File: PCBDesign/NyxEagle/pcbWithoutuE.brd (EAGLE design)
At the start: 100 x 80 mm, 17 parts, among them IC1 DRV8304SRHAR

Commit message: Update pcbWithoutuE.brd and pcbWithoutuE.sch
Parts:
- added IN, IN1, JP1, SPI: (no value), jumper:JP4
- R1, R2: value 10k -> 5.1k
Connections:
- new net CAL: IC1.31, JP1.1
- new net ENABLE: IC1.30, JP1.2
- new net INHA: IC1.34, IN.1
- new net INHB: IC1.36, IN.3
- new net INHC: IC1.38, IN1.1
- new net INLA: IC1.35, IN.2
- new net INLB: IC1.37, IN.4
- new net INLC: IC1.39, IN1.2
- new net N$6: IN1.3
- new net N$7: JP1.4
- new net N$8: IN1.4
- new net NSCS: IC1.29, SPI.1
- new net SCLK: IC1.28, SPI.2
- new net SDI: IC1.27, SPI.3
- net NFAULT: now also JP1.3
- net SDO: now also SPI.4
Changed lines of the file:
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@@
 <attribute name="SPICEPREFIX" value="C" x="2.54" y="-20.32" size="1.778" layer="27" display="off"/>
 </element>
-<element name="R1" library="rcl" library_urn="urn:adsk.eagle:library:334" package="R0805" package3d_urn="urn:adsk.eagle:package:23553/2" value="10k" x="2.54" y="-26.67">
+<element name="R1" library="rcl" library_urn="urn:adsk.eagle:library:334" package="R0805" package3d_urn="urn:adsk.eagle:package:23553/2" value="5.1k" x="2.54" y="-26.67">
 <attribute name="SPICEPREFIX" value="R" x="2.54" y="-26.67" size="1.778" layer="27" display="off"/>
 </element>
@@
 <attribute name="SPICEPREFIX" value="C" x="2.54" y="-33.02" size="1.778" layer="27" display="off"/>
 </element>
-<element name="R2" library="rcl" library_urn="urn:adsk.eagle:library:334" package="R0805" package3d_urn="urn:adsk.eagle:package:23553/2" value="10k" x="2.54" y="-39.37">
+<element name="R2" library="rcl" library_urn="urn:adsk.eagle:library:334" package="R0805" package3d_urn="urn:adsk.eagle:package:23553/2" value="5.1k" x="2.54" y="-39.37">
 <attribute name="SPICEPREFIX" value="R" x="2.54" y="-39.37" size="1.778" layer="27" display="off"/>
 </element>
@@
 <element name="U$5" library="SamacSys_Parts2" package="SI7852ADPT1GE3" value="SIRA80DP-T1-RE3-CLASSIC" x="-25.4" y="-90.17"/>
 <element name="U$6" library="SamacSys_Parts2" package="SI7852ADPT1GE3" value="SIRA80DP-T1-RE3-CLASSIC" x="-33.02" y="-97.79"/>
+<element name="JP1" library="jumper" library_urn="urn:adsk.eagle:library:252" package="JP4" package3d_urn="urn:adsk.eagle:package:15463/1" value="" x="-39.37" y="-105.41"/>
+<element name="SPI" library="jumper" library_urn="urn:adsk.eagle:library:252" package="JP4" package3d_urn="urn:adsk.eagle:package:15463/1" value="" x="-39.37" y="-113.03"/>
+<element name="IN" library="jumper" library_urn="urn:adsk.eagle:library:252" package="JP4" package3d_urn="urn:adsk.eagle:package:15463/1" value="" x="-39.37" y="-120.65"/>
+<element name="IN1" library="jumper" library_urn="urn:adsk.eagle:library:252" package="JP4" package3d_urn="urn:adsk.eagle:package:15463/1" value="" x="-39.37" y="-128.27"/>
 </elements>
 <signals>
@@
 <signal name="NFAULT">
 <contactref element="IC1" pad="25"/>
+<contactref element="JP1" pad="3"/>
+<wire x1="13.11" y1="45.47" x2="-38.1" y2="-105.41" width="0" layer="19" extent="1-1"/>
 </signal>
 <signal name="SDO">
 <contactref element="IC1" pad="26"/>
 <contactref element="R2" pad="1"/>
-<wire x1="1.59" y1="-39.37" x2="13.11" y2="45.97" width="0" layer="19" extent="1-1"/>
+<contactref element="SPI" pad="4"/>
+<wire x1="1.59" y1="-39.37" x2="-35.56" y2="-113.03" width="0" layer="19" extent="1-1"/>
+<wire x1="13.11" y1="45.97" x2="1.59" y2="-39.37" width="0" layer="19" extent="1-1"/>
 </signal>
 <signal name="GHA">
@@
 <wire x1="11.41" y1="42.77" x2="-35.83" y2="-99.695" width="0" layer="19" extent="1-1"/>
 </signal>
+<signal name="N$7">
+<contactref element="JP1" pad="4"/>
+</signal>
+<signal name="CAL">
+<contactref element="IC1" pad="31"/>
+<contactref element="JP1" pad="1"/>
+<wire x1="12.41" y1="48.67" x2="-43.18" y2="-105.41" width="0" layer="19" extent="1-1"/>
+</signal>
+<signal name="ENABLE">
+<contactref element="IC1" pad="30"/>
+<contactref element="JP1" pad="2"/>
+<wire x1="13.11" y1="47.97" x2="-40.64" y2="-105.41" width="0" layer="19" extent="1-1"/>
+</signal>
+<signal name="NSCS">
+<contactref element="SPI" pad="1"/>
+<contactref element="IC1" pad="29"/>
+<wire x1="13.11" y1="47.47" x2="-43.18" y2="-113.03" width="0" layer="19" extent="1-1"/>
+</signal>
+<signal name="SCLK">
+<contactref element="SPI" pad="2"/>
+<contactref element="IC1" pad="28"/>
+<wire x1="13.11" y1="46.97" x2="-40.64" y2="-113.03" width="0" layer="19" extent="1-1"/>
+</signal>
+<signal name="SDI">
+<contactref element="SPI" pad="3"/>
+<contactref element="IC1" pad="27"/>
+<wire x1="13.11" y1="46.47" x2="-38.1" y2="-113.03" width="0" layer="19" extent="1-1"/>
+</signal>
+<signal name="INLC">
+<contactref element="IC1" pad="39"/>
+<contactref element="IN1" pad="2"/>
+<wire x1="8.41" y1="48.67" x2="-40.64" y2="-128.27" width="0" layer="19" extent="1-1"/>
+</signal>
+<signal name="INHC">
+<contactref element="IC1" pad="38"/>
+<contactref element="IN1" pad="1"/>
+<wire x1="8.91" y1="48.67" x2="-43.18" y2="-128.27" width="0" layer="19" extent="1-1"/>
+</signal>
+<signal name="INLB">
+<contactref element="IC1" pad="37"/>
+<contactref element="IN" pad="4"/>
+<wire x1="9.41" y1="48.67" x2="-35.56" y2="-120.65" width="0" layer="19" extent="1-1"/>
+</signal>
+<signal name="INHB">
+<contactref element="IC1" pad="36"/>
+<contactref element="IN" pad="3"/>
+<wire x1="9.91" y1="48.67" x2="-38.1" y2="-120.65" width="0" layer="19" extent="1-1"/>
+</signal>
+<signal name="INLA">
+<contactref element="IC1" pad="35"/>
+<contactref element="IN" pad="2"/>
+<wire x1="10.41" y1="48.67" x2="-40.64" y2="-120.65" width="0" layer="19" extent="1-1"/>
+</signal>
+<signal name="INHA">
+<contactref element="IC1" pad="34"/>
+<contactref element="IN" pad="1"/>
+<wire x1="10.91" y1="48.67" x2="-43.18" y2="-120.65" width="0" layer="19" extent="1-1"/>
+</signal>
+<signal name="N$6">
+<contactref element="IN1" pad="3"/>
+</signal>
+<signal name="N$8">
+<contactref element="IN1" pad="4"/>
+</signal>
 </signals>

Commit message: Update pcbWithoutuE.brd and pcbWithoutuE.sch
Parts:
- added ADCO: (no value), jumper:JP4
- added INPUT, OUT1, OUT2, OUT3: (no value), wirepad:SMD1,27-2,54
- added R3, R4, R5: (no value), resistor_mod:C5931
- moved U$6 200.2 mm to (83.8, 64.8)
- moved U$5 196.9 mm to (83.8, 73.7), turned to 180 degrees
- moved JP1 178.5 mm to (34.3, 57.1), turned to 90 degrees
- moved SPI 175.0 mm to (34.3, 45.7), turned to 90 degrees
- moved IN 171.6 mm to (34.3, 34.3), turned to 270 degrees
- moved IN1 167.0 mm to (34.3, 21.6), turned to 270 degrees
- moved U$4 160.7 mm to (83.8, 41.9)
- moved U$3 159.0 mm to (83.8, 53.3), turned to 180 degrees
- moved C6 140.4 mm to (77.2, 73.2), turned to 90 degrees
- moved C7 126.7 mm to (77.2, 52.8), turned to 90 degrees
- moved U$2 121.2 mm to (83.8, 17.8)
- moved U$1 118.8 mm to (83.8, 29.2), turned to 180 degrees
- moved C8 111.0 mm to (77.0, 29.0), turned to 90 degrees
- moved R2 105.7 mm to (45.7, 57.1)
- moved C5 93.9 mm to (47.8, 49.3)
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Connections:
- new net N$10: ADCO.4
- new net SNA: IC1.10, R3.P$1
- new net SNB: IC1.11, R4.P$1
- new net SNC: IC1.20, R5.P$1
- new net SOA: ADCO.1, IC1.23
- new net SOB: ADCO.2, IC1.22
- new net SOC: ADCO.3, IC1.21
- new net SPA: IC1.9, R3.P$2, U$2.1, U$2.2, U$2.3
- new net SPB: IC1.12, R4.P$2, U$4.1, U$4.2, U$4.3
- new net SPC: IC1.19, R5.P$2, U$6.1, U$6.2, U$6.3
- net +3V3: now also IC1.33
- net SHA: now also OUT1.1
- net SHB: now also OUT2.1
- net SHC: now also OUT3.1
- net VM: now also INPUT.1

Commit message: Update pcbWithoutuE.brd and pcbWithoutuE.sch
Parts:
- moved R1 1.52 mm to (45.7, 53.6)
- moved C5 0.80 mm to (47.5, 50.0)
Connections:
- removed net NFAULT\: R1.1
- net NFAULT: now also R1.1
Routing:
- net SOC: track 0.00 -> 40.9 mm
- net SOB: track 0.00 -> 39.1 mm
- net SOA: track 0.00 -> 37.7 mm
- net SDO: track 0.00 -> 24.3 mm, vias 0 -> 1
- net NFAULT: track 0.00 -> 21.4 mm, vias 0 -> 1
- net ENABLE: track 0.00 -> 20.6 mm, vias 0 -> 1
- net CAL: track 0.00 -> 15.8 mm, vias 0 -> 2
- net NSCS: track 0.00 -> 14.0 mm
- net SCLK: track 0.00 -> 12.9 mm
- net SDI: track 0.00 -> 12.1 mm
- net +3V3: track 0.00 -> 11.1 mm

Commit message: Update pcbWithoutuE.brd
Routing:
- net GHC: track 0.00 -> 73.5 mm, vias 0 -> 2
- net SHA: track 0.00 -> 65.4 mm, vias 0 -> 2
- net GLA: track 0.00 -> 64.3 mm
- net GHB: track 0.00 -> 61.4 mm
- net SPA: track 0.00 -> 55.0 mm
- net SHC: track 0.00 -> 53.0 mm
- net SPC: track 0.00 -> 49.8 mm
- net GHA: track 0.00 -> 49.4 mm, vias 0 -> 2
- net GLC: track 0.00 -> 48.7 mm
- net SNC: track 0.00 -> 45.8 mm
- net SHB: track 0.00 -> 43.8 mm
- net GLB: track 0.00 -> 40.3 mm, vias 0 -> 2
- net SPB: track 0.00 -> 33.2 mm, vias 0 -> 4
- net SNB: track 0.00 -> 29.6 mm, vias 0 -> 2
- net SNA: track 0.00 -> 27.7 mm
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- added copper zone on layer 1, net SHA
- added copper zone on layer 1, net SHB
- added copper zone on layer 1, net SHC

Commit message: Update pcbWithoutuE.brd and pcbWithoutuE.sch
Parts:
- added GND: (no value), wirepad:SMD1,27-2,54
- added R10, R9: (no value), rcl:R0201
- added R6, R7: 0, rcl:R0805W
- added R8: 0, rcl:R0201
- moved C4 1.60 mm to (49.6, 23.4)
- moved C3 0.76 mm to (49.5, 19.3)
- moved INPUT 0.09 mm to (47.2, 12.1)
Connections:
- new net AGND: C3.-, C4.2, C6.2, C7.2, C8.2, GND.1, R10.1, R3.P$1, R4.P$1, R5.P$1, R6.1, R7.1, R8.1, R9.1
- net GND: now also R6.2, R7.2; no longer C3.-, C4.2, C6.2, C7.2, C8.2
- net SNA: now also R8.2; no longer R3.P$1
- net SNB: now also R9.2; no longer R4.P$1
- net SNC: now also R10.2; no longer R5.P$1
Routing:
- net VM: track 8.42 -> 198.7 mm, vias 0 -> 12
- net AGND: track 0.00 -> 49.5 mm, vias 0 -> 26
- net GHB: track 61.4 -> 49.5 mm
- net SNB: track 29.6 -> 22.0 mm
- net SPA: track 55.0 -> 61.6 mm
- net GND: track 0.00 -> 5.94 mm, vias 0 -> 12
- net SHC: track 53.0 -> 58.3 mm
- net SHB: track 43.8 -> 48.7 mm
- net SPB: track 33.2 -> 37.9 mm, vias 4 -> 2
- net SHA: track 65.4 -> 60.9 mm
- net SNC: track 45.8 -> 41.5 mm
- net SNA: track 27.7 -> 24.5 mm
- net GLC: track 48.7 -> 48.1 mm
- added copper zone on layer 1, net AGND
- added copper zone on layer 16, net AGND
- added copper zone on layer 16, net GND
- added copper zone on layer 1, net SPA
- added copper zone on layer 1, net SPB

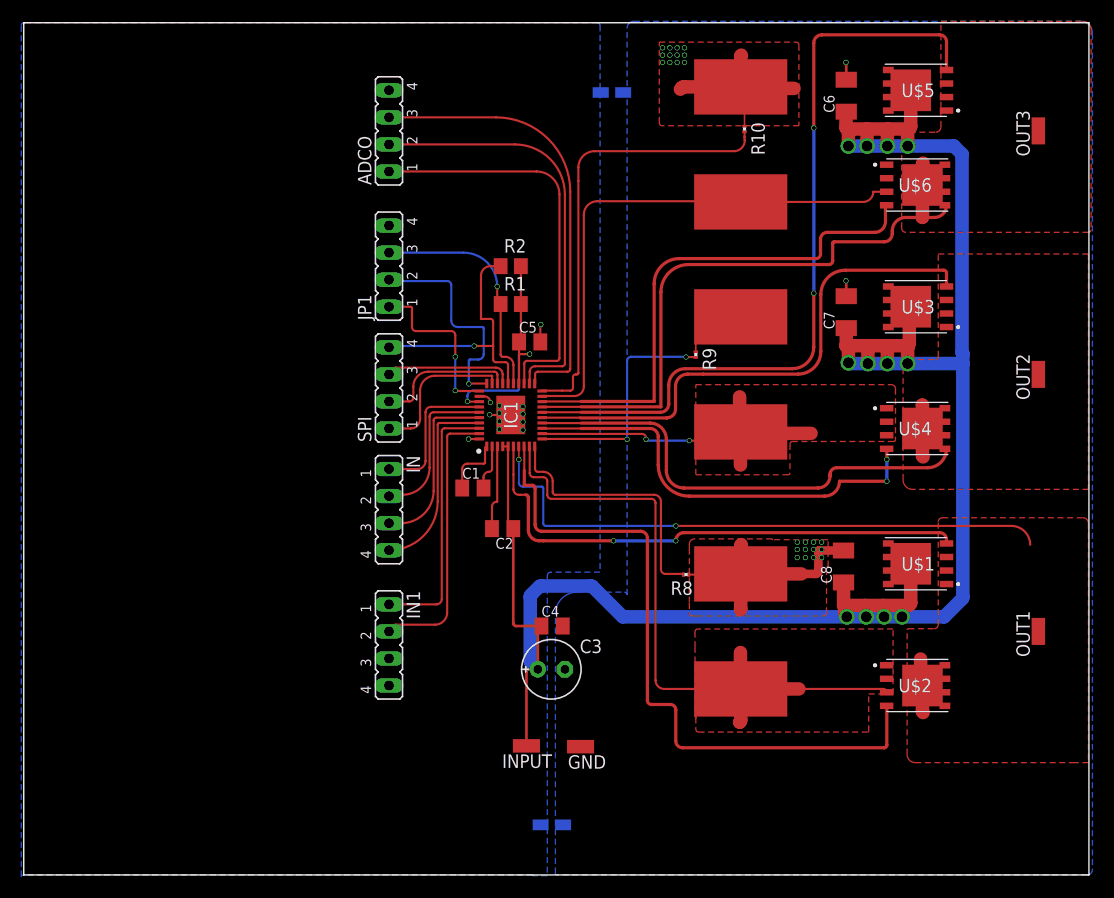
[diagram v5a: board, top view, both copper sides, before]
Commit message: Change of shunt resistors to smaller.
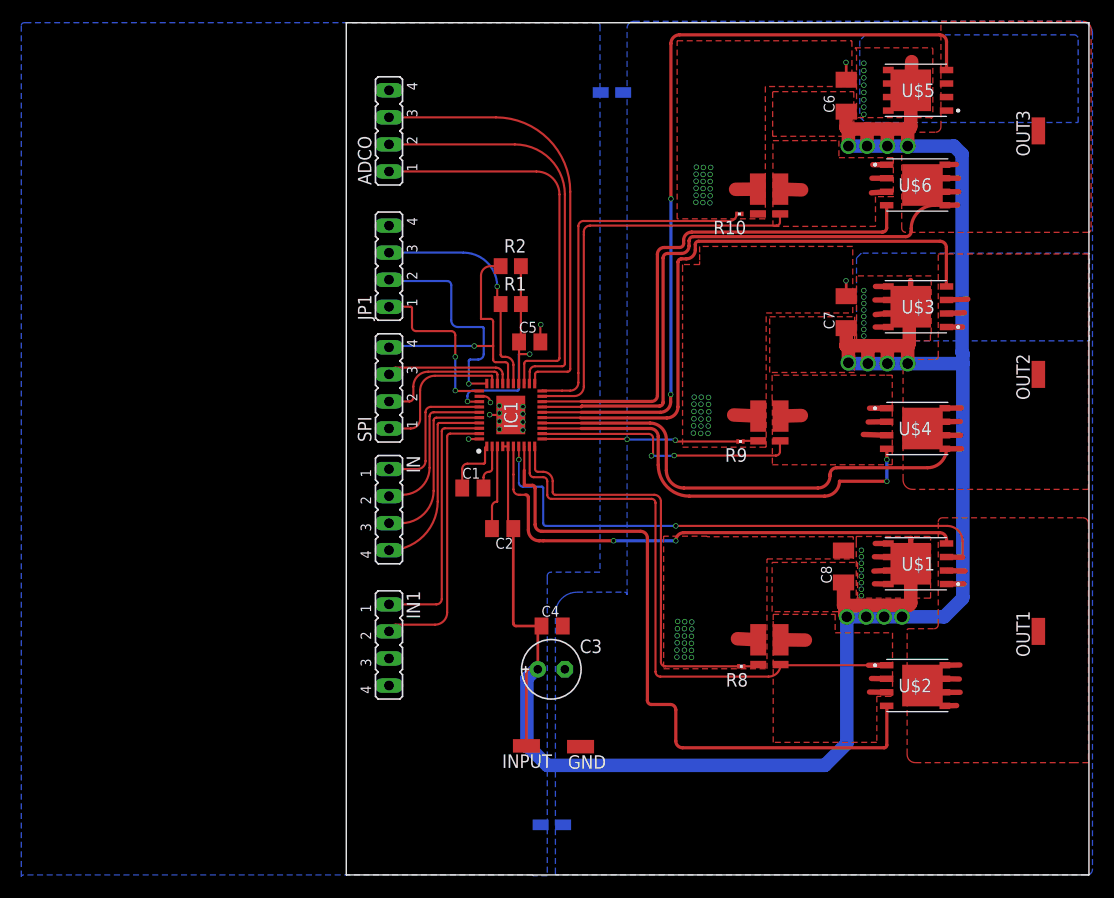
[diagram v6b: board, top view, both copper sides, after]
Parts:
- R3, R4, R5: value (none) -> 1mOhm; device resistor_mod:C5931 -> resistor_mod:1216
- moved R8 10.0 mm to (67.4, 19.6)
- moved R9 9.17 mm to (67.3, 40.7), turned to 180 degrees
- moved R10 7.99 mm to (67.2, 62.1), turned to 180 degrees
- moved R5 6.82 mm to (70.0, 62.3), turned to 180 degrees
- moved R4 6.57 mm to (70.0, 41.0), turned to 180 degrees
- moved R3 3.93 mm to (70.0, 20.0), turned to 180 degrees
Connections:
- removed net N$7: JP1.4
- net AGND: now also R3.P$2, R3.P$4, R4.P$2, R4.P$4, R5.P$2, R5.P$4; no longer R3.P$1, R4.P$1, R5.P$1
- net GND: now also JP1.4
- net SPA: now also R3.P$1, R3.P$3; no longer R3.P$2
- net SPB: now also R4.P$1, R4.P$3; no longer R4.P$2
- net SPC: now also R5.P$1, R5.P$3; no longer R5.P$2
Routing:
- net AGND: track 49.5 -> 12.3 mm, vias 26 -> 56
- net VM: track 198.7 -> 227.8 mm, vias 12 -> 37
- net SNA: track 24.5 -> 38.3 mm
- net SNC: track 41.5 -> 33.7 mm
- net GHB: track 49.5 -> 57.0 mm
- net SHB: track 48.7 -> 54.4 mm
- net SPC: track 49.8 -> 44.5 mm
- net SPB: track 37.9 -> 33.1 mm
- net SNB: track 22.0 -> 18.5 mm
- net GHC: track 73.3 -> 75.3 mm
- net SPA: track 61.6 -> 59.8 mm
- net GLC: track 48.1 -> 49.3 mm
- added copper zone on layer 1, net SPC
- added copper zone on layer 1, net VM
- added copper zone on layer 16, net VM
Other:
- board size 100 x 80 mm -> 69.7 x 80 mm

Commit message: PCB is ready and before the silk layer.
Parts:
- C3: device rcl:E2,5-6E -> rcl:E7,5-16
- GND, INPUT: device wirepad:SMD1,27-2,54 -> wirepad:3,17/1,3
- moved R7 16.9 mm to (42.5, 20.1)
- moved INPUT 11.4 mm to (58.4, 14.4)
- moved GND 2.43 mm to (51.8, 14.4)
- moved C4 2.39 mm to (52.0, 23.7), turned to 180 degrees
- moved C3 2.16 mm to (51.4, 20.3), turned to 180 degrees
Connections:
- removed net N$10: ADCO.4
- removed net N$6: IN1.3
- removed net N$8: IN1.4
- net GND: now also ADCO.4, IN1.3, IN1.4
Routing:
- net VM: track 227.8 -> 210.2 mm, vias 37 -> 36
- net AGND: track 12.3 -> 26.1 mm, vias 56 -> 57
- net GLA: track 64.4 -> 63.9 mm
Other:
- board size 69.7 x 80 mm -> 69.9 x 73.4 mm
- board text added: "CAL"
- board text added: "DGND"
- board text added: "ENABLE"
- board text added: "INHA"
- board text added: "INHB"
- board text added: "INHC"
- board text added: "INLA"
- board text added: "INLB"
- board text added: "INlC"
- board text added: "NC"
- board text added: "NFAULT"
- board text added: "NSCS"
- board text added: "SCLK"
- board text added: "SDI"
- board text added: "SDO"
- board text added: "SOA"
- board text added: "SOB"
- board text added: "SOC"

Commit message: Silk layer is ready
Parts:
- moved GND 4.09 mm to (51.9, 10.3)
- moved INPUT 3.87 mm to (58.7, 10.5)
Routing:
- net AGND: track 26.1 -> 30.2 mm
- net SHA: track 60.7 -> 63.2 mm
- net SHB: track 54.4 -> 56.8 mm
- net SHC: track 58.4 -> 60.7 mm
- net VM: track 210.2 -> 211.3 mm
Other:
- board text added: "ADCO"
- board text added: "C1"
- board text added: "C2"
- board text added: "C3"
- board text added: "C4"
- board text added: "C5"
- board text added: "C6"
- board text added: "C7"
- board text added: "C8"
- board text added: "GND"
- board text added: "IC1"
- board text added: "INPUT"
- board text added: "OUT1"
- board text added: "OUT2"
- board text added: "OUT3"
- board text added: "R1"
- board text added: "R2"
- board text added: "SPI"
